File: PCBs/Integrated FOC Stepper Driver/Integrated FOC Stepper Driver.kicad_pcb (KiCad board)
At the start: 6 copper layers, 40 x 40 mm, 67 parts, among them J1 USB C Receptacle, J2 Conn_01x03, J3 INPUT, J4 OUTPUT, J5 Conn_01x02, J6 MOTOR, SW1 BTN, SW2 BTN, U1 RP2040, U2 W25Q128JVS, U3 PJ54M50SE, U4 PJ9500M33SA, U5 SN65HVD1050D, U8 MT6701CT, Y1 ABM8-272-T3

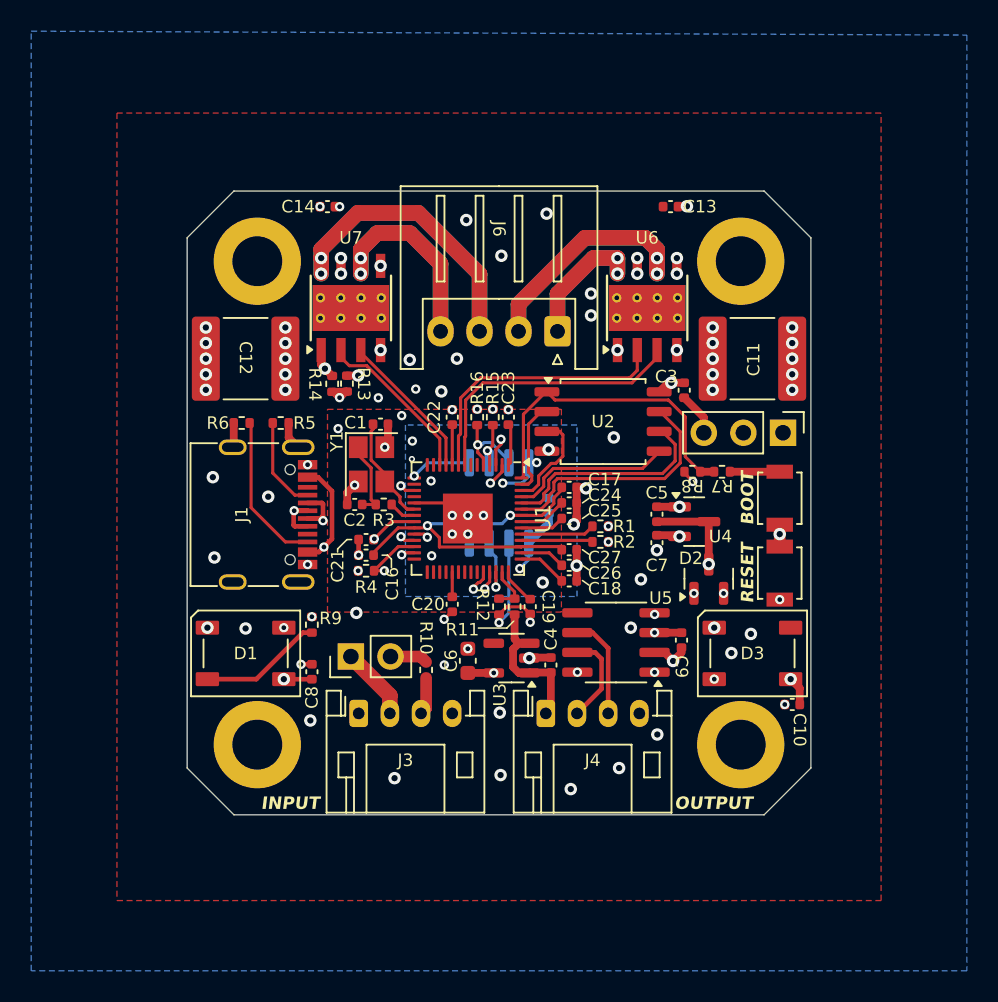
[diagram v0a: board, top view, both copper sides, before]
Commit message: Switch to 0805 capacitors instead of stacked 2220 capacitors
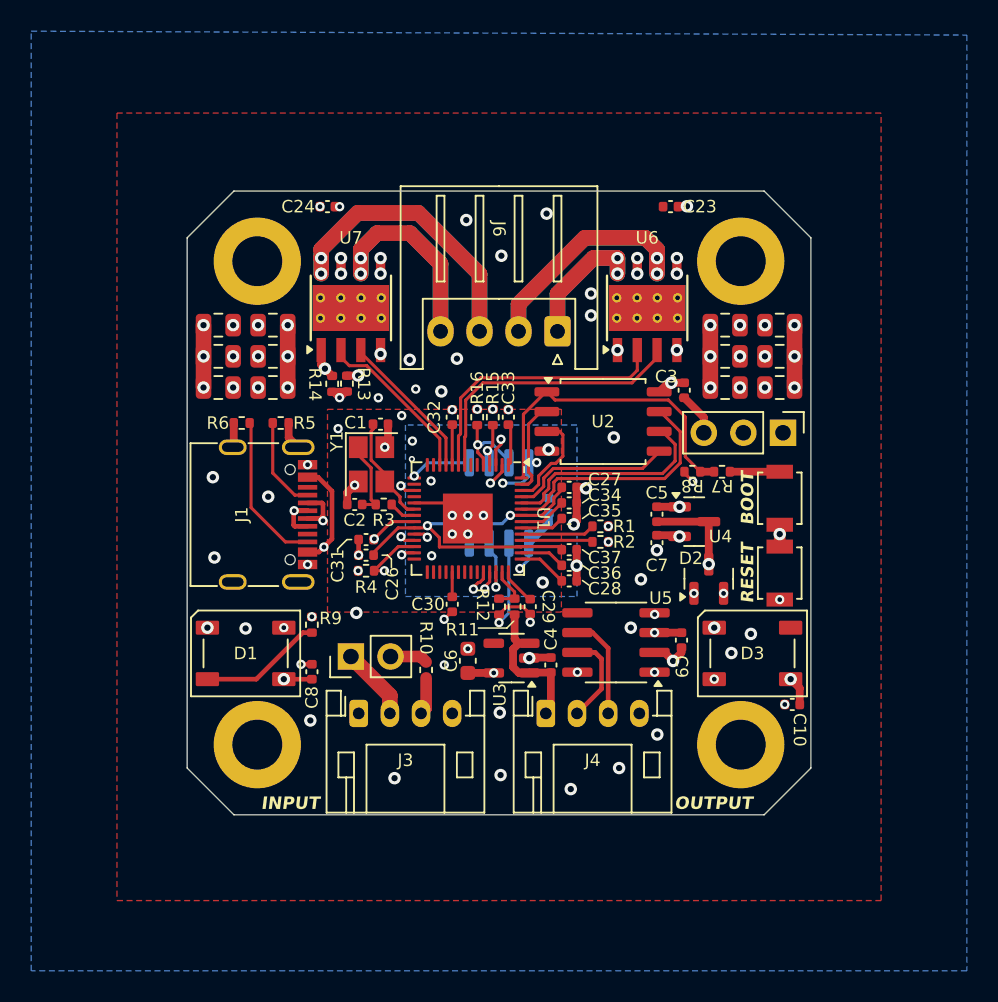
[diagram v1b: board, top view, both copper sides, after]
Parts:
- added C11: 10uF, Capacitor_SMD:C_0805_2012Metric, F.Cu at (64.5, 38.6)
- added C13: 10uF, Capacitor_SMD:C_0805_2012Metric, F.Cu at (64.5, 40.6)
- added C14: 10uF, Capacitor_SMD:C_0805_2012Metric, F.Cu at (35.5, 40.6)
- added C15: 10uF, Capacitor_SMD:C_0805_2012Metric, F.Cu at (64.5, 42.6)
- added C16: 10uF, Capacitor_SMD:C_0805_2012Metric, F.Cu at (35.5, 42.6)
- added C17: 10uF, Capacitor_SMD:C_0805_2012Metric, F.Cu at (68.0, 38.6)
- added C18: 10uF, Capacitor_SMD:C_0805_2012Metric, F.Cu at (32.0, 38.6)
- added C19: 10uF, Capacitor_SMD:C_0805_2012Metric, F.Cu at (68.0, 40.6)
- added C20: 10uF, Capacitor_SMD:C_0805_2012Metric, F.Cu at (32.0, 40.6)
- added C22: 10uF, Capacitor_SMD:C_0805_2012Metric, F.Cu at (32.0, 42.6)
- C12: value 47uF -> 10uF; footprint Capacitor_SMD:C_2220_5750Metric -> Capacitor_SMD:C_0805_2012Metric
- C21: renamed from C11; value 47uF -> 10uF; footprint Capacitor_SMD:C_2220_5750Metric -> Capacitor_SMD:C_0805_2012Metric
- moved C12 2.77 mm to (35.5, 38.6)
- moved C21 2.55 mm to (68.0, 42.6), turned to 180 degrees
- renumbered C13 to C23, C14 to C24, C15 to C25, C16 to C26, C17 to C27, C18 to C28, C19 to C29, C20 to C30, C21 to C31, C22 to C32, C23 to C33, C24 to C34, C25 to C35, C26 to C36, C27 to C37
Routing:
- net VBUS: track 99.5 -> 154.3 mm, vias 19 -> 22
- net GND: vias 72 -> 74

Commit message: (did not ctrl+s sorry)
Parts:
- C25: footprint Capacitor_SMD:C_0402_1005Metric -> Capacitor_SMD:C_0603_1608Metric
- moved C23 1.86 mm to (61.4, 32.8), turned to 90 degrees
- moved C24 1.16 mm to (39.0, 32.2)
- moved C25 0.44 mm to (53.6, 50.0)
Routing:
- net VBUS: track 154.3 -> 153.9 mm, vias 22 -> 21
- net GND: vias 74 -> 75
